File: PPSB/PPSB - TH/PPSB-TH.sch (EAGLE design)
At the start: 4 parts

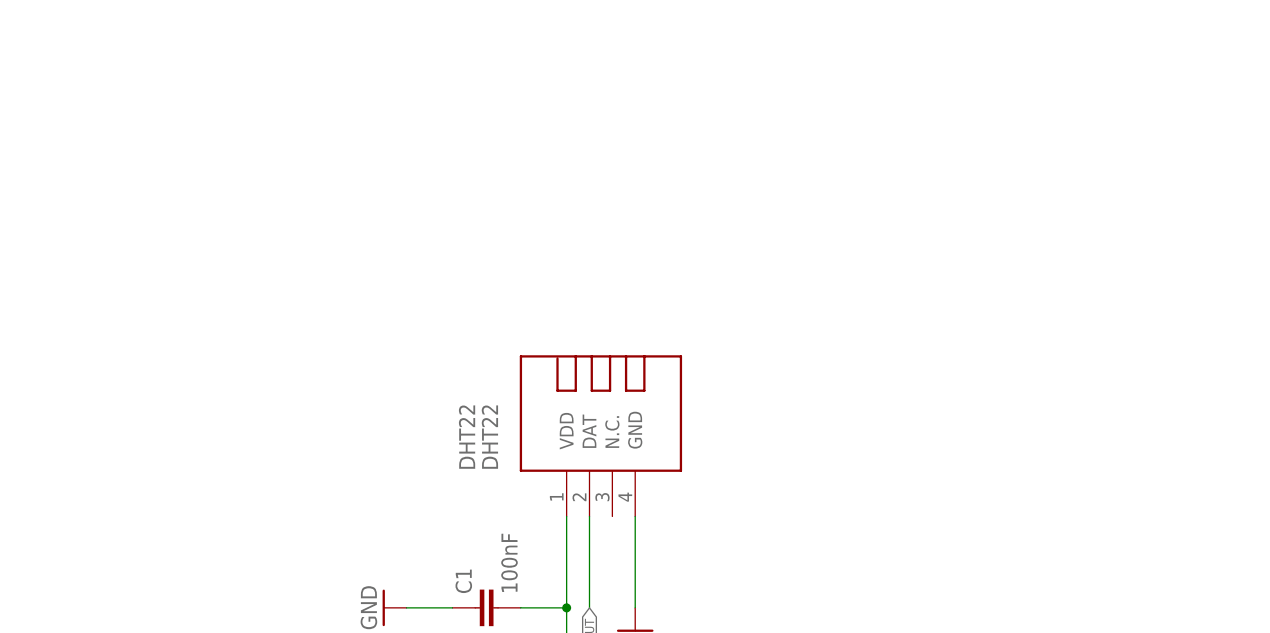
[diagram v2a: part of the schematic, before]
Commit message: Improved schematics layout.
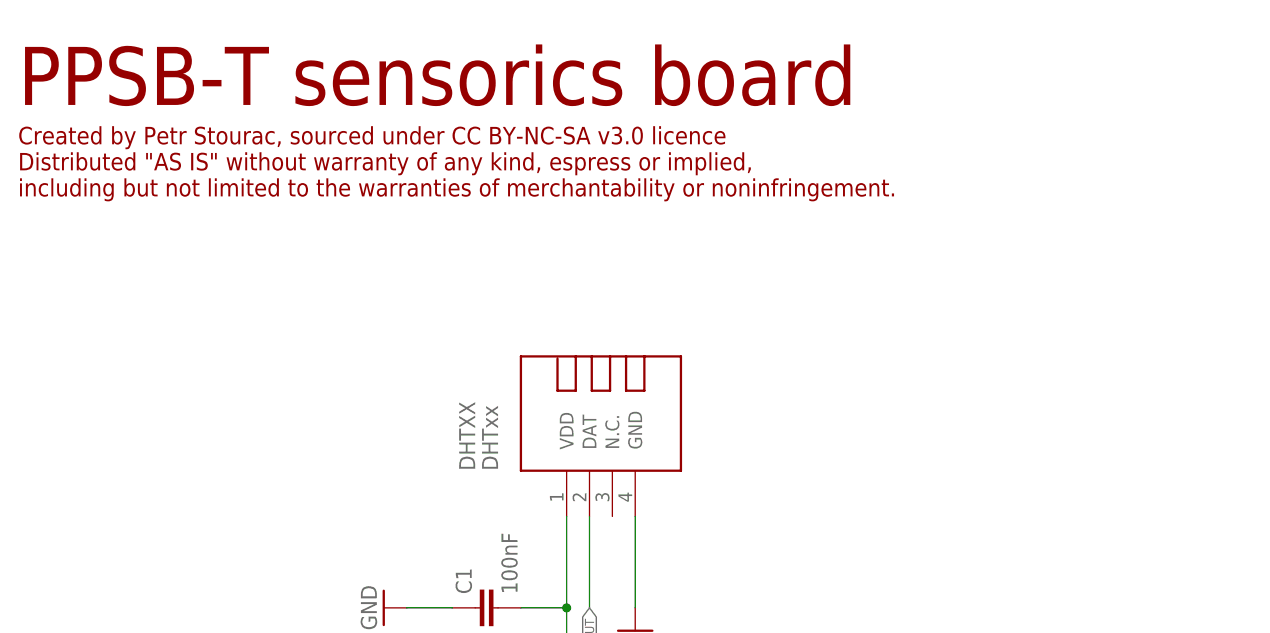
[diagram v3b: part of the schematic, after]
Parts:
- DHTXX: value DHT22 -> DHTxx
- renumbered DHT22 to DHTXX
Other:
- note added: "Created by Petr Stourac, sourced under CC BY-NC-SA v3.0 licence Distributed "AS IS" without warranty of any kind, espress or implied, including but not limited to the warranties of merchantability or noninfringement."
- note added: "PPSB-T sensorics board"
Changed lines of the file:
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@@
 </classes>
 <parts>
-<part name="DHT22" library="diy-modules" deviceset="TEMP-HUM-SENSOR-DHT22" device="" value="DHT22"/>
+<part name="DHTXX" library="diy-modules" deviceset="TEMP-HUM-SENSOR-DHT22" device="" override_package3d_urn="urn:adsk.eagle:package:19743369/2" override_package_urn="urn:adsk.eagle:footprint:19743370/1" value="DHTxx"/>
 <part name="GND1" library="supply1" library_urn="urn:adsk.eagle:library:371" deviceset="GND" device=""/>
 <part name="GND2" library="supply1" library_urn="urn:adsk.eagle:library:371" deviceset="GND" device=""/>
@@
 <part name="FRAME1" library="frames" library_urn="urn:adsk.eagle:library:229" deviceset="A5P-LOC" device=""/>
 <part name="C1" library="rcl" library_urn="urn:adsk.eagle:library:334" deviceset="C-EU" device="C0603" package3d_urn="urn:adsk.eagle:package:23616/2" value="100nF"/>
-<part name="CON" library="#PaJa_konektory" deviceset="ARK500/3" device=""/>
+<part name="CON" library="#PaJa_konektory" library_urn="urn:adsk.eagle:library:19754563" deviceset="ARK500/3" device="" package3d_urn="urn:adsk.eagle:package:19754722/2"/>
 <part name="T_CON" library="pinhead" library_urn="urn:adsk.eagle:library:325" deviceset="PINHD-1X3" device="" package3d_urn="urn:adsk.eagle:package:22458/2"/>
 <part name="GND3" library="supply1" library_urn="urn:adsk.eagle:library:371" deviceset="GND" device=""/>
@@
 <sheet>
 <plain>
+<text x="7.62" y="165.1" size="6.4516" layer="94">PPSB-T sensorics board</text>
+<text x="7.62" y="154.94" size="1.9304" layer="94">Created by Petr Stourac, sourced under CC BY-NC-SA v3.0 licence
+Distributed "AS IS" without warranty of any kind, espress or implied,
+including but not limited to the warranties of merchantability or noninfringement.</text>
 </plain>
 <instances>
-<instance part="DHT22" gate="G$1" x="73.66" y="132.08" smashed="yes" rot="R90">
+<instance part="DHTXX" gate="G$1" x="73.66" y="132.08" smashed="yes" rot="R90">
 <attribute name="NAME" x="58.42" y="124.46" size="1.778" layer="95" rot="R90"/>
 <attribute name="VALUE" x="60.96" y="124.46" size="1.778" layer="95" rot="R90"/>
@@
 <net name="GND" class="0">
 <segment>
-<pinref part="DHT22" gate="G$1" pin="GND"/>
+<pinref part="DHTXX" gate="G$1" pin="GND"/>
 <wire x1="76.2" y1="119.38" x2="76.2" y2="109.22" width="0.1524" layer="91"/>
 <pinref part="GND1" gate="1" pin="GND"/>
@@
 <net name="DATA_OUT" class="0">
 <segment>
-<pinref part="DHT22" gate="G$1" pin="DAT"/>
+<pinref part="DHTXX" gate="G$1" pin="DAT"/>
 <wire x1="71.12" y1="119.38" x2="71.12" y2="109.22" width="0.1524" layer="91"/>
 <label x="71.12" y="109.22" size="1.016" layer="95" rot="R270" xref="yes"/>
@@
 <net name="+5V" class="0">
 <segment>
-<pinref part="DHT22" gate="G$1" pin="VDD"/>
+<pinref part="DHTXX" gate="G$1" pin="VDD"/>
 <wire x1="68.58" y1="119.38" x2="68.58" y2="109.22" width="0.1524" layer="91"/>
 <pinref part="P+1" gate="1" pin="+5V"/>
@@
 </drawing>
 <compatibility>
+<note version="6.3" minversion="6.2.2" severity="warning">
+Since Version 6.2.2 text objects can contain more than one line,
+which will not be processed correctly with this version.
+</note>
 <note version="8.2" severity="warning">
 Since Version 8.2, EAGLE supports online libraries. The ids
@@
 packages will not be understood (or retained) with this version.
 </note>
+<note version="9.4" severity="warning">
+Since Version 9.4, EAGLE supports the overriding of 3D packages
+in schematics and board files. Those overridden 3d packages
+will not be understood (or retained) with this version.
+</note>
 <note version="8.4" severity="warning">

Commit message: Update schematics
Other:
- note added: "ver. 1 rev. 1"
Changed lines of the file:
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@@
 <setting verticaltext="up"/>
 </settings>
-<grid distance="0.1" unitdist="inch" unit="inch" style="lines" multiple="1" display="no" altdistance="0.01" altunitdist="inch" altunit="inch"/>
+<grid distance="0.1" unitdist="inch" unit="inch" style="lines" multiple="1" display="yes" altdistance="0.01" altunitdist="inch" altunit="inch"/>
 <layers>
 <layer number="1" name="Top" color="4" fill="1" visible="no" active="no"/>
@@
 Distributed "AS IS" without warranty of any kind, espress or implied,
 including but not limited to the warranties of merchantability or noninfringement.</text>
+<text x="87.376" y="20.32" size="2.54" layer="94">ver. 1 rev. 1</text>
 </plain>
 <instances>
